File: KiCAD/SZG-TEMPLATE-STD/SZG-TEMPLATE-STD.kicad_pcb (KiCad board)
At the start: 4 copper layers, 45 x 70 mm, 30 parts, among them J1 SYZYGY_STD, J2 Conn_01x06, U1 ATtiny44A-MU

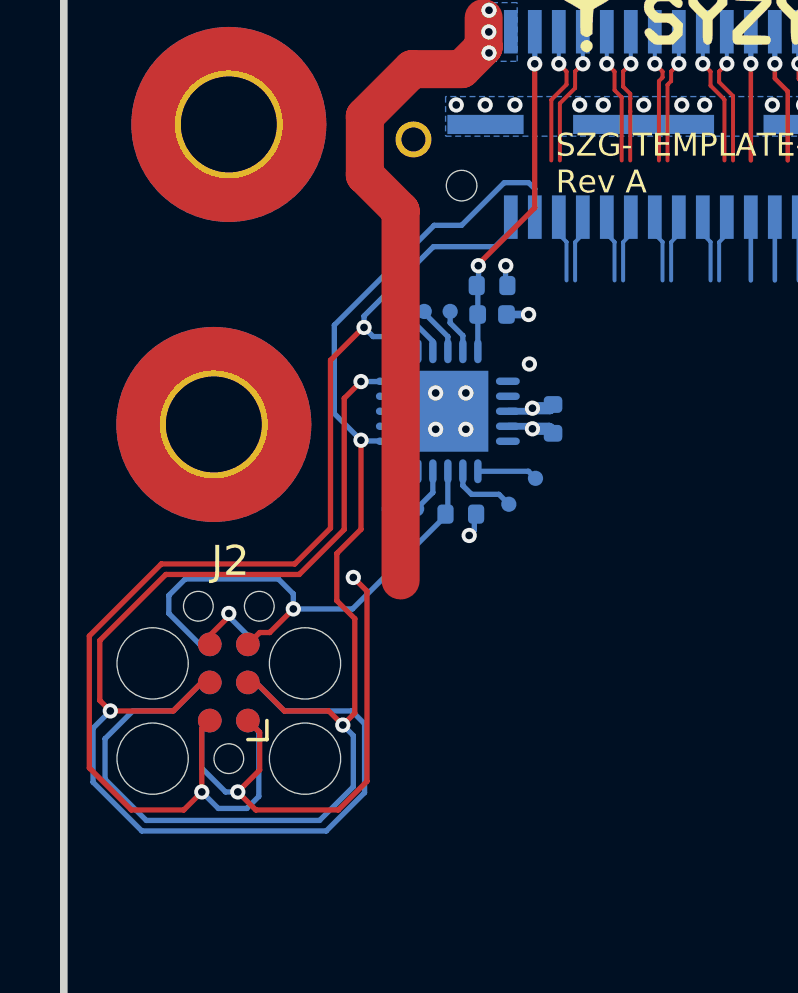
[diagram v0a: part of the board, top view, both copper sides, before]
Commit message: Updated the template projects MCU programming header to use the standard Tag-Connect cable pin order.
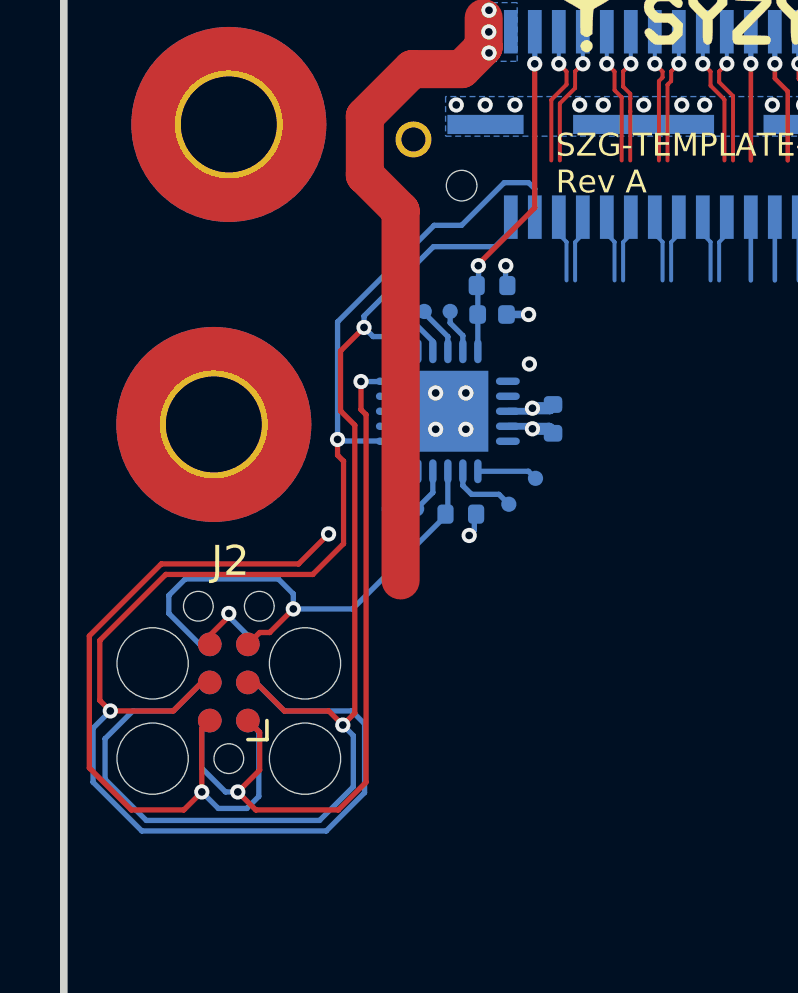
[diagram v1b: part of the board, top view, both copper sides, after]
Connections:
- J2 pad 1: +3V3 -> /MCU_MISO
- J2 pad 2: /MCU_SCL_USCK -> +3V3
- J2 pad 3: /MCU_SDA_MOSI -> /MCU_SCL_USCK
- J2 pad 4: /MCU_MISO -> /MCU_SDA_MOSI
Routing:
- net /MCU_MISO: track 41.6 -> 25.3 mm
- net /MCU_SDA_MOSI: track 46.1 -> 54.0 mm
- net +3V3: track 63.6 -> 71.4 mm
- net /MCU_SCL_USCK: track 42.1 -> 44.0 mm

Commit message: Updated SZG-TEMPLATE-STD to KiCAD v6. Added STD port silk logo.
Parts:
- added REF**: SYZYGY_STD_Logo, SYZYGY:SYZYGY_STD_Logo, F.Cu at (128.5, 62.0)
- moved FID4 9.85 mm to (122.2, 70.6)
- moved FID5 9.85 mm to (122.2, 70.6)
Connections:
- H1 pad 1: Net-(H1-Pad1) -> (no net)
- H2 pad 1: Net-(H2-Pad1) -> (no net)
- H3 pad 1: Net-(H3-Pad1) -> (no net)
- H4 pad 1: Net-(H4-Pad1) -> (no net)
- H5 pad 1: Net-(H5-Pad1) -> (no net)
- H6 pad 1: Net-(H6-Pad1) -> (no net)
- U1 pad 10: Net-(U1-Pad10) -> (no net)
- U1 pad 17: Net-(U1-Pad17) -> (no net)
- U1 pad 18: Net-(U1-Pad18) -> (no net)
- U1 pad 19: Net-(U1-Pad19) -> (no net)
- U1 pad 6: Net-(U1-Pad6) -> (no net)
- U1 pad 7: Net-(U1-Pad7) -> (no net)
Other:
- net class Default removed
